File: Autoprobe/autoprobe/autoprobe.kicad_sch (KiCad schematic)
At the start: 9 parts, among them J1 Conn_01x09, J2 Conn_01x05, J3 Molex 502494-0470, U1 M24C02-FMN

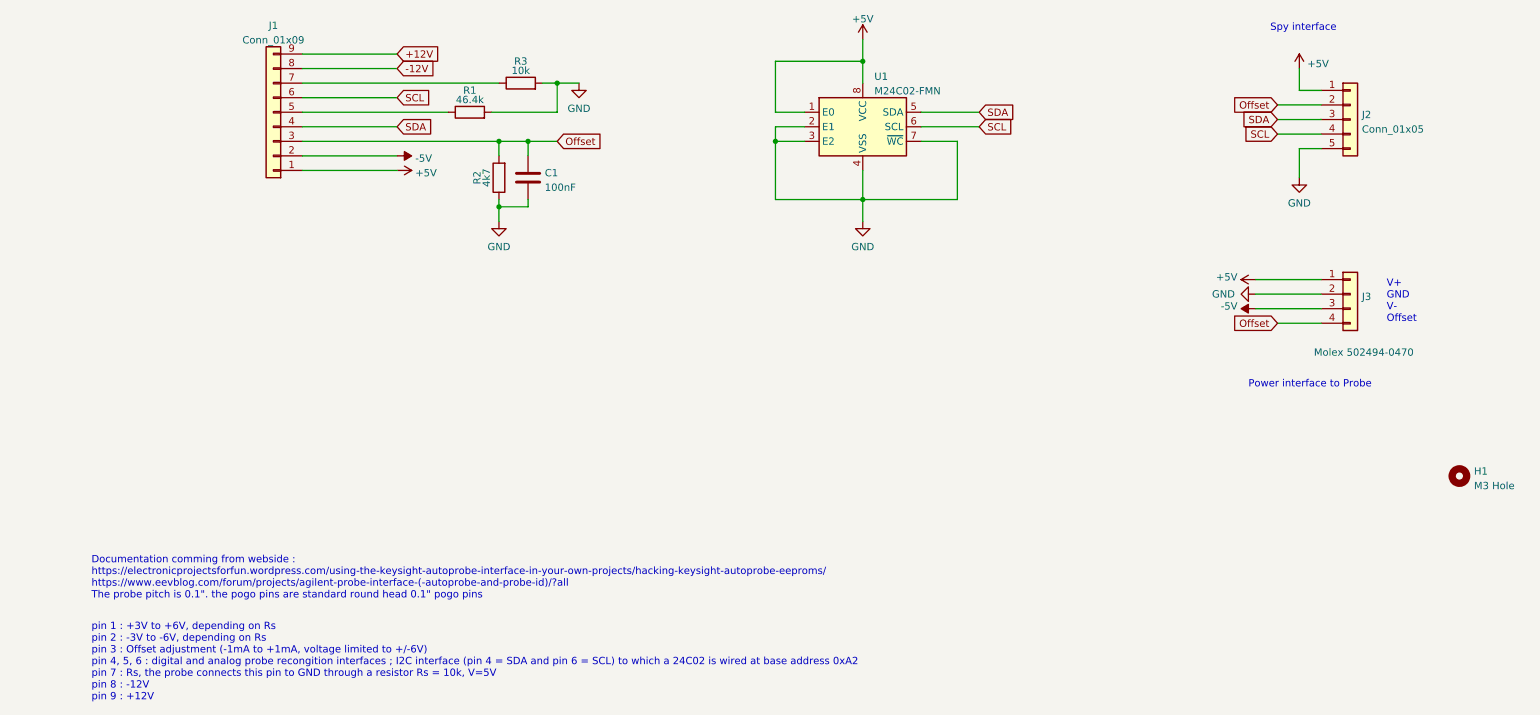
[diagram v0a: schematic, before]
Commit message: Update Autoprobe project to the Kicad 9.xx Add some Bin files for the EEPROM data add some documentation files
Update the High speed diff probe Kicad data
change the silkscreen - more reasonable position
Add the Project Name, an revision on the PCB board.
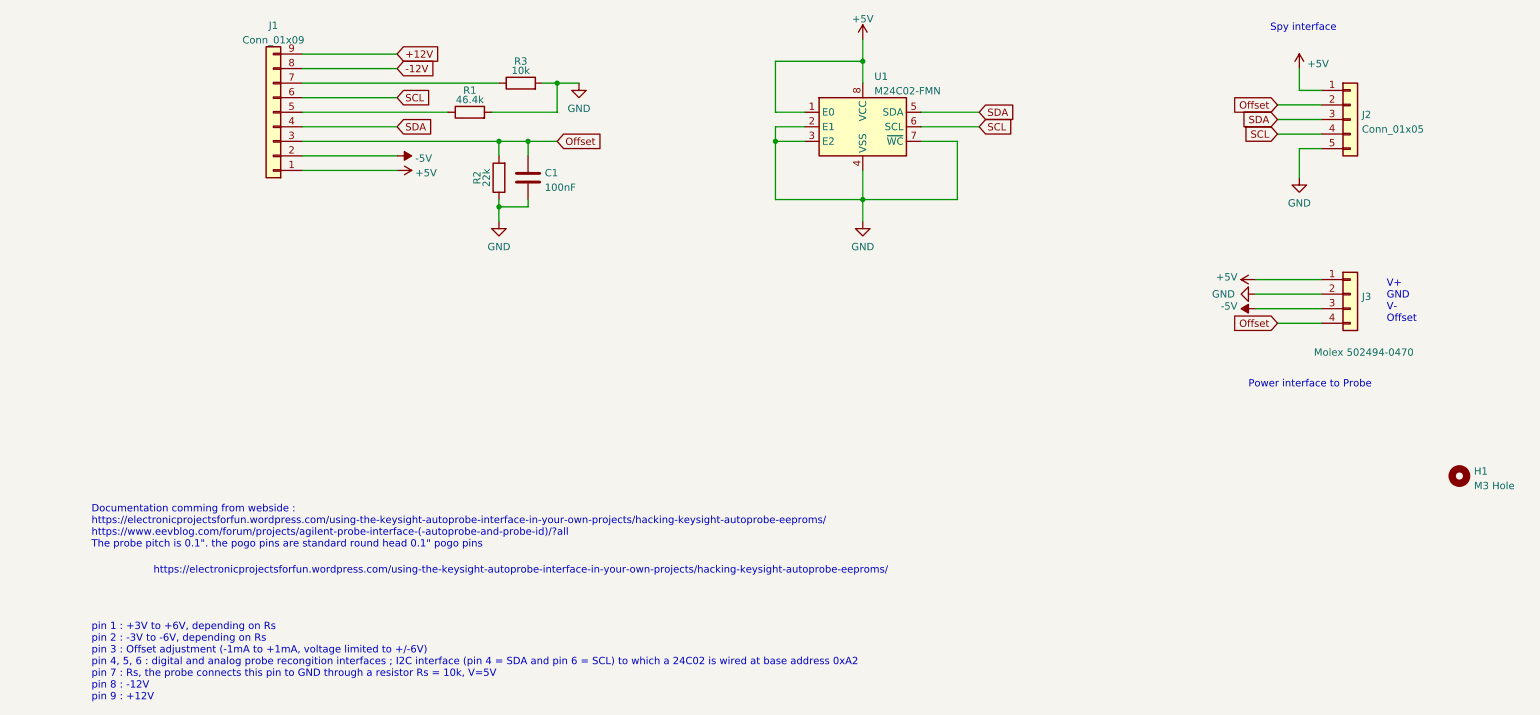
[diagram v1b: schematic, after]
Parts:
- R2: value 4k7 -> 22k
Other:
- note added: "https://electronicprojectsforfun.wordpress.com/using-the-keysight-autoprobe-interface-in-your-own-projects/hacking-keysight-autoprobe-eeproms/"
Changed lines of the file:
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@@
 (kicad_sch
-	(version 20231120)
+	(version 20250114)
 	(generator "eeschema")
-	(generator_version "8.0")
+	(generator_version "9.0")
 	(paper "A4")
 	(title_block
@@
 		(rev "0.1")
 	)
+	(text "https://electronicprojectsforfun.wordpress.com/using-the-keysight-autoprobe-interface-in-your-own-projects/hacking-keysight-autoprobe-eeproms/"
+		(exclude_from_sim no)
+		(at 95.25 168.91 0)
+		(effects
+			(font
+				(size 1.27 1.27)
+			)
+			(href "https://electronicprojectsforfun.wordpress.com/using-the-keysight-autoprobe-interface-in-your-own-projects/hacking-keysight-autoprobe-eeproms/")
+		)
+	)
+	(text "pin 1 : +3V to +6V, depending on Rs\npin 2 : -3V to -6V, depending on Rs\npin 3 : Offset adjustment (-1mA to +1mA, voltage limited to +/-6V)\npin 4, 5, 6 : digital and analog probe recongition interfaces ; I2C interface (pin 4 = SDA and pin 6 = SCL) to which a 24C02 is wired at base address 0xA2\npin 7 : Rs, the probe connects this pin to GND through a resistor Rs = 10k, V=5V\npin 8 : -12V\npin 9 : +12V"
+		(exclude_from_sim no)
+		(at 20.32 191.77 0)
+		(effects
+			(font
+				(size 1.27 1.27)
+			)
+			(justify left bottom)
+		)
+	)
+	(text "Documentation comming from webside :\nhttps://electronicprojectsforfun.wordpress.com/using-the-keysight-autoprobe-interface-in-your-own-projects/hacking-keysight-autoprobe-eeproms/\nhttps://www.eevblog.com/forum/projects/agilent-probe-interface-(-autoprobe-and-probe-id)/?all\nThe probe pitch is 0.1\". the pogo pins are standard round head 0.1\" pogo pins"
+		(exclude_from_sim no)
+		(at 20.32 165.1 0)
+		(effects
+			(font
+				(size 1.27 1.27)
+			)
+			(justify left bottom)
+			(href "https://www.eevblog.com/forum/projects/agilent-probe-interface-(-autoprobe-and-probe-id)/?all")
+		)
+	)
+	(text "V+\nGND\nV-\nOffset"
+		(exclude_from_sim no)
+		(at 246.38 125.73 0)
+		(effects
+			(font
+				(size 1.27 1.27)
+			)
+			(justify left bottom)
+		)
+	)
+	(text "Power interface to Probe"
+		(exclude_from_sim no)
+		(at 222.25 137.16 0)
+		(effects
+			(font
+				(size 1.27 1.27)
+			)
+			(justify left bottom)
+		)
+	)
+	(text "Spy interface"
+		(exclude_from_sim no)
+		(at 226.06 74.93 0)
+		(effects
+			(font
+				(size 1.27 1.27)
+			)
+			(justify left bottom)
+		)
+	)
 	(junction
 		(at 101.6 83.82)
@@
 			(width 0)
 			(type default)
-		)
-	)
-	(text "pin 1 : +3V to +6V, depending on Rs\npin 2 : -3V to -6V, depending on Rs\npin 3 : Offset adjustment (-1mA to +1mA, voltage limited to +/-6V)\npin 4, 5, 6 : digital and analog probe recongition interfaces ; I2C interface (pin 4 = SDA and pin 6 = SCL) to which a 24C02 is wired at base address 0xA2\npin 7 : Rs, the probe connects this pin to GND through a resistor Rs = 10k, V=5V\npin 8 : -12V\npin 9 : +12V"
-		(exclude_from_sim no)
-		(at 20.32 191.77 0)
-		(effects
-			(font
-				(size 1.27 1.27)
-			)
-			(justify left bottom)
-		)
-	)
-	(text "Documentation comming from webside :\nhttps://electronicprojectsforfun.wordpress.com/using-the-keysight-autoprobe-interface-in-your-own-projects/hacking-keysight-autoprobe-eeproms/\nhttps://www.eevblog.com/forum/projects/agilent-probe-interface-(-autoprobe-and-probe-id)/?all\nThe probe pitch is 0.1\". the pogo pins are standard round head 0.1\" pogo pins"
-		(exclude_from_sim no)
-		(at 20.32 173.99 0)
-		(effects
-			(font
-				(size 1.27 1.27)
-			)
-			(justify left bottom)
-		)
-	)
-	(text "V+\nGND\nV-\nOffset"
-		(exclude_from_sim no)
-		(at 246.38 125.73 0)
-		(effects
-			(font
-				(size 1.27 1.27)
-			)
-			(justify left bottom)
-		)
-	)
-	(text "Power interface to Probe"
-		(exclude_from_sim no)
-		(at 222.25 137.16 0)
-		(effects
-			(font
-				(size 1.27 1.27)
-			)
-			(justify left bottom)
-		)
-	)
-	(text "Spy interface"
-		(exclude_from_sim no)
-		(at 226.06 74.93 0)
-		(effects
-			(font
-				(size 1.27 1.27)
-			)
-			(justify left bottom)
 		)
 	)
@@
 			)
 		)
-		(property "Value" "4k7"
+		(property "Value" "22k"
 			(at 89.2611 100.33 90)
 			(effects
@@
 		)
 	)
+	(embedded_fonts no)
 )
